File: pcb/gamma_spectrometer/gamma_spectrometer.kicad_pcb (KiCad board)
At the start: 2 copper layers, 255 x 45 mm, 228 parts, among them J101 DX07S024WJ3R400, Q201 IRLML0040, Q401 MMBTA42, Q402 MMBTA42, Q403 MMBTA42, T201 ATB322524-0110-T000, U101 LP5907MFX-3.3, U102 AMS1117-3.3, U103 FT231XQ, U104 TPS60400DBV, U201 max1847eee+, U202 TL431, U301 TL431, U302 STM32G474MET6, U303 W25Q64JVSSIQ, U402 ADA4817-1ARDZ, Y301 ABM8G-16.000MHZ-4Y-T3

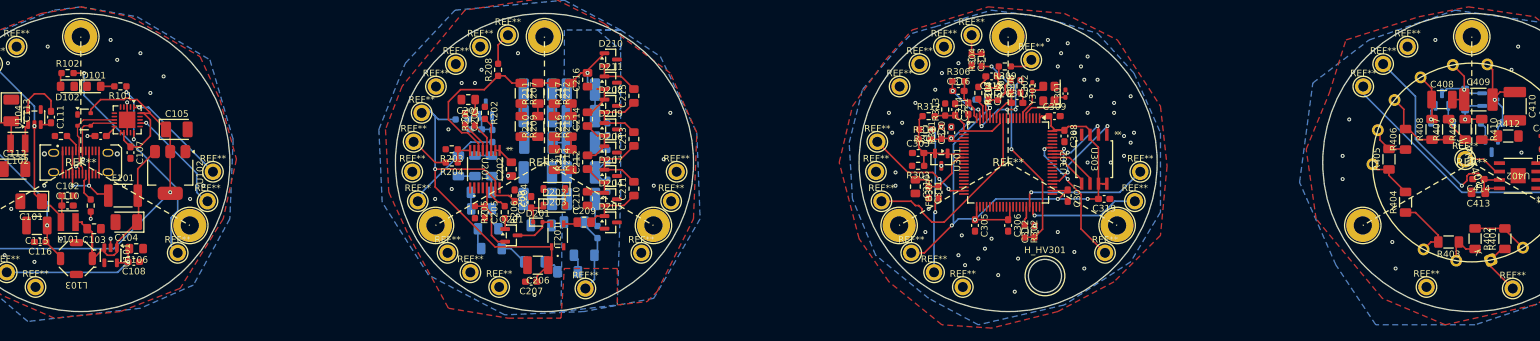
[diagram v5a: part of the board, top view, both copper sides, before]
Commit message: fix: полярность тракта, опора REF35250, DRC по электрике в ноль
ПОЛЯРНОСТЬ (главное). Анод ФЭУ забирает условный ток => выход TIA идёт
вверх => импульс на АЦП положительный. В доках и прошивке была обратная
конвенция, выросшая из sim2_shaper.cir, где источник тока анода развёрнут
(`I_pmt 0 anode` вместо `I_pmt anode 0`); sim_divider_complete.cir всё это
время делал верно — две деки противоречили друг другу.

Последствия при старых смещениях (sim_polarity_headroom.cir, реальная
модель ADA4817): OPAMP1 уходил вниз до -1.09 В при VOLSAT 100 мВ (клиппинг
с ~1.2 МэВ), АЦП вверх до 3.99 В при VREF+ 2.495 (обрезка с ~0.70 МэВ).
Прибор мерил бы до 700 кэВ вместо 3.5 МэВ.

Исправление — два резистора, железо не переделывается:
  R313 2.0к -> 14.7к   V_A 0.490 -> 1.602 В
  R311 5.9к -> 909     V_PB0 0.529 -> 0.099 В, базовая линия АЦП -> 0.408 В
Запасы на потолке 3.5 МэВ (sim_bias_fixed.cir): OPAMP1 0.575..2.515,
OPAMP2 1.580..2.082, АЦП 0.308..2.276 (до VREF+ +0.224 В).
Попутно вскрыто: выход OPAMP1 сидит на 1.5*V_A, а не на V_A — R314 (фикс C2)
создаёт путь по постоянному току в обход C315. Нигде не было записано.
В прошивке остаётся сделать `amplitude = sample - baseline`.

ОПОРА. TL431DBZ -> REF35250QDBVR (SOT-23-6) по итогам ревью инженера:
параметрический шунт заменён последовательной опорой. 12 ppm/°C вместо 50
(у клона YOUTAI до 300), точность ±0.05%. Дрейф калибровки на ±30 °C:
0.9% -> 0.036%. R301 удалён, C303 100нФ -> 1мкФ (обязательный выходной),
добавлен C322 1мкФ на вывод NR. Правило шпаргалки №9 (ток шунта) для U301
больше не применимо; U202 на ВВ-плате остаётся TL431.
⚠ REF35205, который он назвал — это 2.048 В, не подходит (пик 2.118 В).

DRC. По электрике ноль нарушений: clearance, track_dangling, via_dangling,
holes_co_located, starved_thermal — все пусты. Всего 774 -> 402, остаток
целиком шелкография и courtyard.
- 25 GND-падов переведены на сплошное соединение с зоной (стойки, развязка,
  кварц, земля MAX1847, выход опоры)
- экран USB-C заземлён: J101 пер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
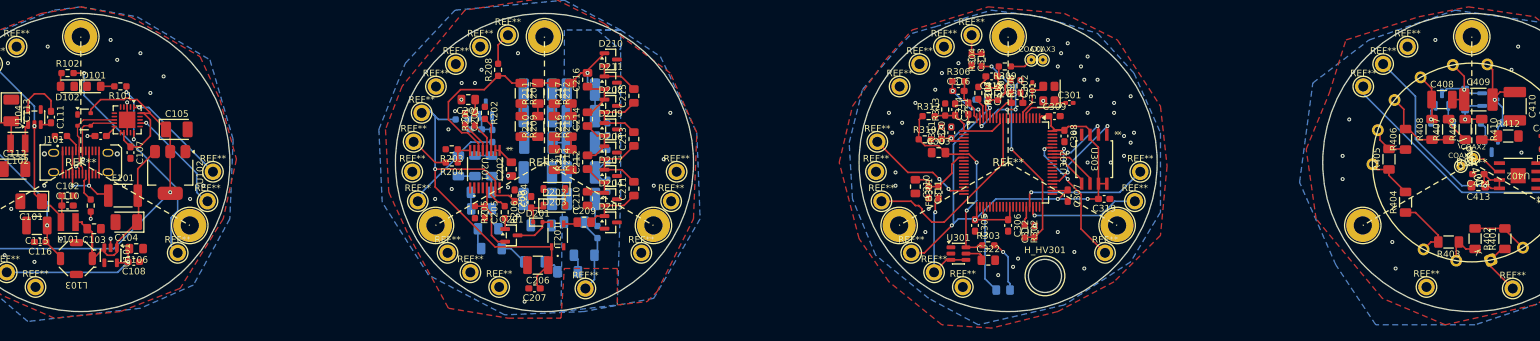
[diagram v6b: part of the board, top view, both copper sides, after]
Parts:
- removed R301: R330, Resistor_SMD:R_0603_1608Metric_Pad0.98x0.95mm_HandSolder
- removed the REF** at (309.0, 99.5)
- removed the REF** at (243.5, 84.5)
- added C322: 1uF, Capacitor_SMD:C_0805_2012Metric_Pad1.18x1.45mm_HandSolder, F.Cu at (237.0, 114.8)
- added COAX1: COAX_PIN_D0.5, COAX_PIN_D0.5, F.Cu at (243.5, 84.5)
- added COAX2: COAX_PIN_D0.5, COAX_PIN_D0.5, F.Cu at (310.2, 99.2)
- added COAX3: COAX_PIN_D0.5, COAX_PIN_D0.5, F.Cu at (245.2, 84.5)
- added COAX4: COAX_PIN_D0.5, COAX_PIN_D0.5, F.Cu at (308.4, 100.5)
- added TP_TSENS301: TP_TSENS_2x0805, TP_TSENS_2x0805, B.Cu at (239.2, 119.2)
- C303: value 0.1uF -> 1uF; footprint Capacitor_SMD:C_0603_1608Metric_Pad1.08x0.95mm_HandSolder -> Capacitor_SMD:C_0805_2012Metric_Pad1.18x1.45mm_HandSolder
- J101: footprint Connector_USB:USB_C_Receptacle_JAE_DX07S024WJ3R400 -> посадочные места:USB_C_Receptacle_JAE_DX07S024WJ3R400
- R311: value 5.9k -> 909R
- R313: value 2k -> 14.7k
- U301: value TL431 -> REF35250QDBVR; footprint Package_TO_SOT_SMD:SOT-23 -> Package_TO_SOT_SMD:SOT-23-6
- moved R303 16.0 mm to (237.0, 112.5), turned to 0 degrees
- moved U301 14.4 mm to (232.5, 113.8), turned to 0 degrees
- moved C303 3.09 mm to (229.5, 98.5)
- moved C301 1.52 mm to (249.2, 91.0), turned to 0 degrees
- moved C207 1.12 mm to (168.5, 119.0)
- moved C413 1.00 mm to (311.0, 103.5)
- moved C414 0.75 mm to (311.0, 101.8)
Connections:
- C303 pad 2: Net-(U301-K) -> Net-(U301-VREF)
- R303 pad 1: Net-(U301-K) -> Net-(U301-VREF)
- R310 pad 1: Net-(U301-K) -> Net-(U301-VREF)
- R312 pad 1: Net-(U301-K) -> Net-(U301-VREF)
- U301 pad 1: Net-(U301-K) -> GND
- U301 pad 2: Net-(U301-K) -> GND
- U301 pad 3: GND -> +3.3V_A
- U302 pad 28: Net-(U301-K) -> Net-(U301-VREF)
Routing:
- net Net-(U301-VREF): track 0.00 -> 29.6 mm, vias 0 -> 2
- net Net-(U301-K): track 14.2 -> 0.00 mm
- net TSENS_IN: track 0.00 -> 13.4 mm, vias 0 -> 1
- net TSENS_PWR: track 0.00 -> 7.93 mm, vias 0 -> 1
- net +3.3V_A: track 47.0 -> 39.9 mm, vias 3 -> 2
- net Net-(U301-NR): track 0.00 -> 3.18 mm
- net Net-(C214-Pad2): track 6.10 -> 7.67 mm
- net +5V_HV: track 89.1 -> 90.3 mm
- net AMP_OUT: track 9.45 -> 8.30 mm
- net +3.3V_D: track 161.7 -> 161.1 mm, vias 7 -> 6
- net GND: vias 96 -> 93

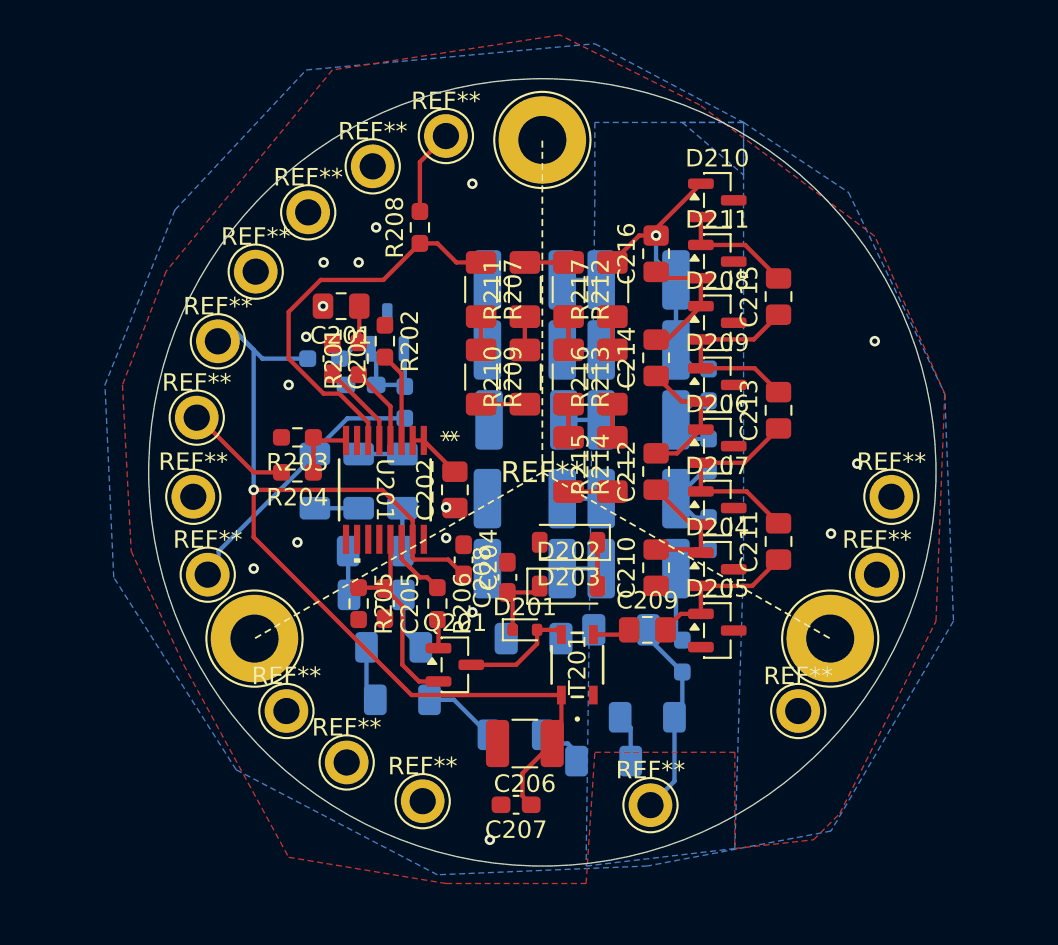
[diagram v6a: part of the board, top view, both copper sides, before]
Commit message: fix(drc): правила ВВ-зазоров глушили проверку целиком — исправлено
НАЙДЕНО ПОЛЬЗОВАТЕЛЕМ. Блок из 12 «исключений» в .kicad_dru для деталей,
соединяющих ВВ-узел с землёй (T201, C210, D205, C410, R412, C13b201..C18b201,
Q403), был написан как `(constraint clearance (min 0mm))` с условием
`insideCourtyard('<ref>')`. Это не освобождает частный случай, а перебивает
остальные правила и ОБНУЛЯЕТ проверку зазора глобально.

Бисекция:
  49 ВВ-правил, без исключений  ->  59 нарушений зазора
  те же 49 + 12 «исключений»    ->   0 нарушений

Полтора дня проект числился «чистым по электрике», хотя заливка GND стояла
в 0.0005 мм от цепи под 908 В (Net-(R211-Pad2), ~168.0/88.5 на ВВ-плате).
Три доклада «нарушений нет» были построены на молчании заглушённого DRC.

Исключения удалены, в файле осталось 49 честных правил + комментарий, почему
блок убран и как решать задачу правильно (точечные исключения DRC в редакторе;
реальных случаев было два — C210 и C18b201).

Побочно вскрылось: `kicad-cli pcb drc` не перезаливает зоны и потому вообще
не проверяет зазоры «зона <-> цепь» и starved_thermal. Для всего, что связано
с заливкой, — только встроенный DRC в Pcbnew.

Записано правилом №13 в cheatsheet_mistakes.md с методикой проверки:
подозрительное правило убрать и посмотреть, не выросло ли число находок;
тишина DRC не доказательство, пока контрольным опытом не показано, что он
способен найти нарушение в этом месте.

Документация приведена в соответствие:
- session_context: шапка «СОСТОЯНИЕ НА 2026-08-08» для восстановления после
  сжатия — состояние схемы/платы, честный счёт DRC, три грабли инструмента,
  приоритеты работ, рабочие приёмы. Прежние выводы «нарушений 0» помечены ⛔.
  Заодно вычищены управляющие байты, из-за которых git считал файл бинарным.
- CLAUDE.md, README(.en): статус разводки — 59 мест к переделке, а не «чисто».

Co-Authored-By: Claude Opus 5 (1M context) <noreply@anthropic.com>
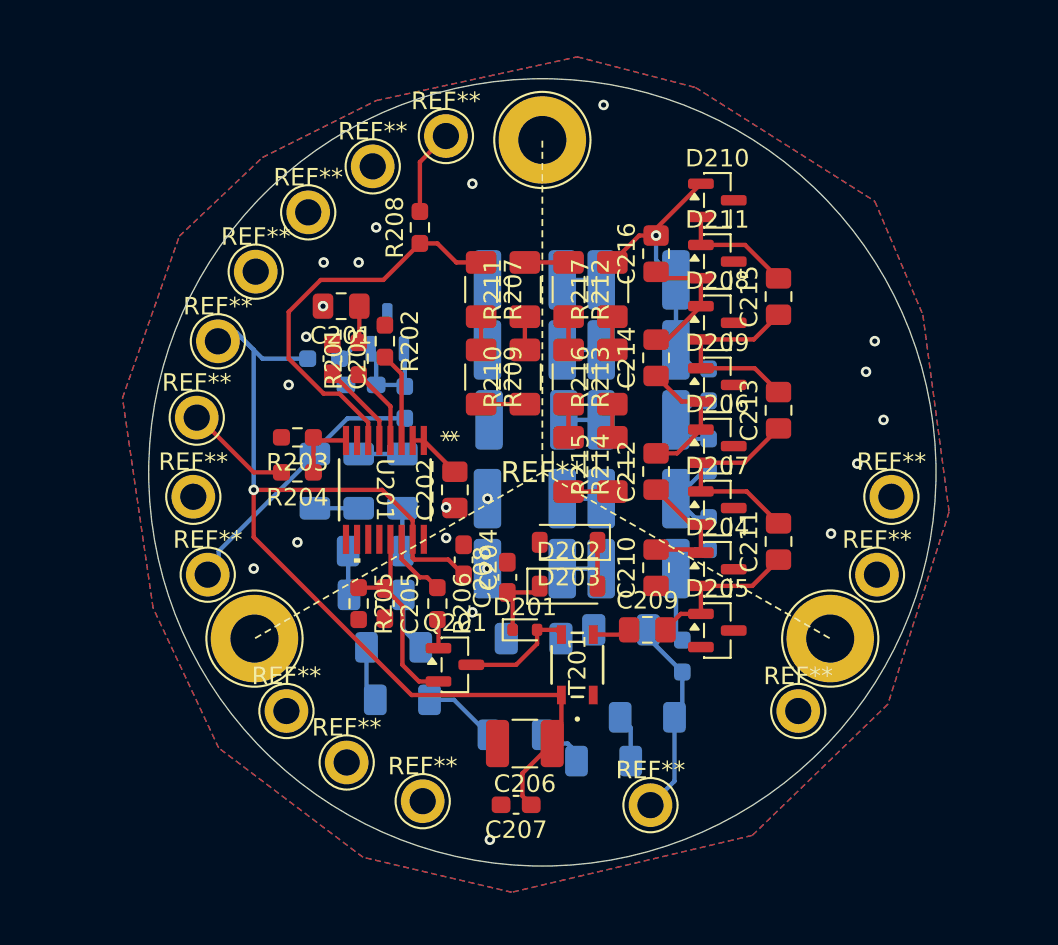
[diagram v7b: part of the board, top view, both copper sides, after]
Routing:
- net GND: vias 93 -> 98
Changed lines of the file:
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@@
 	)
 	(via
+		(at 173.5 79)
+		(size 0.6)
+		(drill 0.3)
+		(layers "F.Cu" "B.Cu")
+		(free yes)
+		(net 3)
+	)
+	(via
 		(at 330 100.5)
 		(size 0.6)
@@
 	)
 	(via
+		(at 166.8625 105.5)
+		(size 0.6)
+		(drill 0.3)
+		(layers "F.Cu" "B.Cu")
+		(net 3)
+	)
+	(via
 		(at 118.5 103.5)
 		(size 0.6)
@@
 	)
 	(via
+		(at 189.5 97)
+		(size 0.6)
+		(drill 0.3)
+		(layers "F.Cu" "B.Cu")
+		(free yes)
+		(net 3)
+	)
+	(via
 		(at 298.5 116)
 		(size 0.6)
@@
 	)
 	(via
+		(at 188.5 94.25)
+		(size 0.6)
+		(drill 0.3)
+		(layers "F.Cu" "B.Cu")
+		(free yes)
+		(net 3)
+	)
+	(via
 		(at 224 94)
 		(size 0.6)
@@
 	)
 	(via
+		(at 166.8625 101.5)
+		(size 0.6)
+		(drill 0.3)
+		(layers "F.Cu" "B.Cu")
+		(net 3)
+	)
+	(via
 		(at 94.5 103.5)
 		(size 0.6)
@@
 		(layer "F.Cu")
 		(hatch edge 0.5)
-		(priority 4)
-		(connect_pads
-			(clearance 0.5)
-		)
-		(min_thickness 0.25)
-		(filled_areas_thickness no)
-		(fill yes
-			(thermal_gap 0.5)
-			(thermal_bridge_width 0.5)
-		)
-		(polygon
-			(pts
-				(xy 173 116) (xy 181 116) (xy 181 121.5) (xy 185.5 121) (xy 187 119.5) (xy 192.5 108.5) (xy 193 95.5)
-				(xy 189 86.5) (xy 179 79) (xy 171 75) (xy 158 77) (xy 148.5 88.5) (xy 146 95) (xy 146.5 104.5) (xy 149.5 111)
-				(xy 155.5 122) (xy 164.5 123.5) (xy 172.5 123.5)
-			)
-		)
-	)
-	(zone
-		(net 3)
-		(net_name "GND")
-		(layer "F.Cu")
-		(hatch edge 0.5)
 		(priority 7)
 		(connect_pads
@@
 		(net 3)
 		(net_name "GND")
-		(layer "B.Cu")
+		(layers "F.Cu" "B.Cu")
 		(hatch edge 0.5)
 		(priority 2)
@@
 		(polygon
 			(pts
-				(xy 178 80) (xy 181.5 83) (xy 181.5 80)
+				(xy 149.25 86.5) (xy 154 82) (xy 160.5 78.75) (xy 172 76.25) (xy 178.75 78) (xy 189 84.5) (xy 191.75 91)
+				(xy 193.25 102.25) (xy 189.75 113.25) (xy 182 120.75) (xy 168.25 124) (xy 159.75 122) (xy 151.5 115.75)
+				(xy 147.75 107.75) (xy 146 95.75)
 			)
 		)
@@
 			)
 		)
-	)
-	(zone
-		(net 3)
-		(net_name "GND")
-		(layer "B.Cu")
-		(hatch edge 0.5)
-		(priority 6)
-		(connect_pads
-			(clearance 0.5)
-		)
-		(min_thickness 0.25)
-		(filled_areas_thickness no)
-		(fill yes
-			(thermal_gap 0.5)
-			(thermal_bridge_width 0.5)
-		)
-		(polygon
-			(pts
-				(xy 173 84.5) (xy 172.5 122.5) (xy 181 121.5) (xy 181.5 105) (xy 181.5 91.5) (xy 181.5 80) (xy 187.5 84)
-				(xy 193 95.5) (xy 193.5 108.5) (xy 186.5 120.5) (xy 176 122.5) (xy 164 123) (xy 152.5 117) (xy 145.5 106)
-				(xy 145 95) (xy 149 85) (xy 156.5 77) (xy 173 75.5) (xy 181.5 80) (xy 173 80)
-			)
-		)
